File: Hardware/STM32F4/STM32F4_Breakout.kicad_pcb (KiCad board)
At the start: 4 copper layers, 68 x 59 mm, 50 parts, among them J1 Screw_Terminal_01x02, J2 SWD, J3 Conn_01x04, J4 Conn_01x04, J5 USB_B, Q1 AO3401A, SW1 SW_SPDT, U1 STM32F405RGT6, U2 MP2303ADN, U3 USBLC6-2SC6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

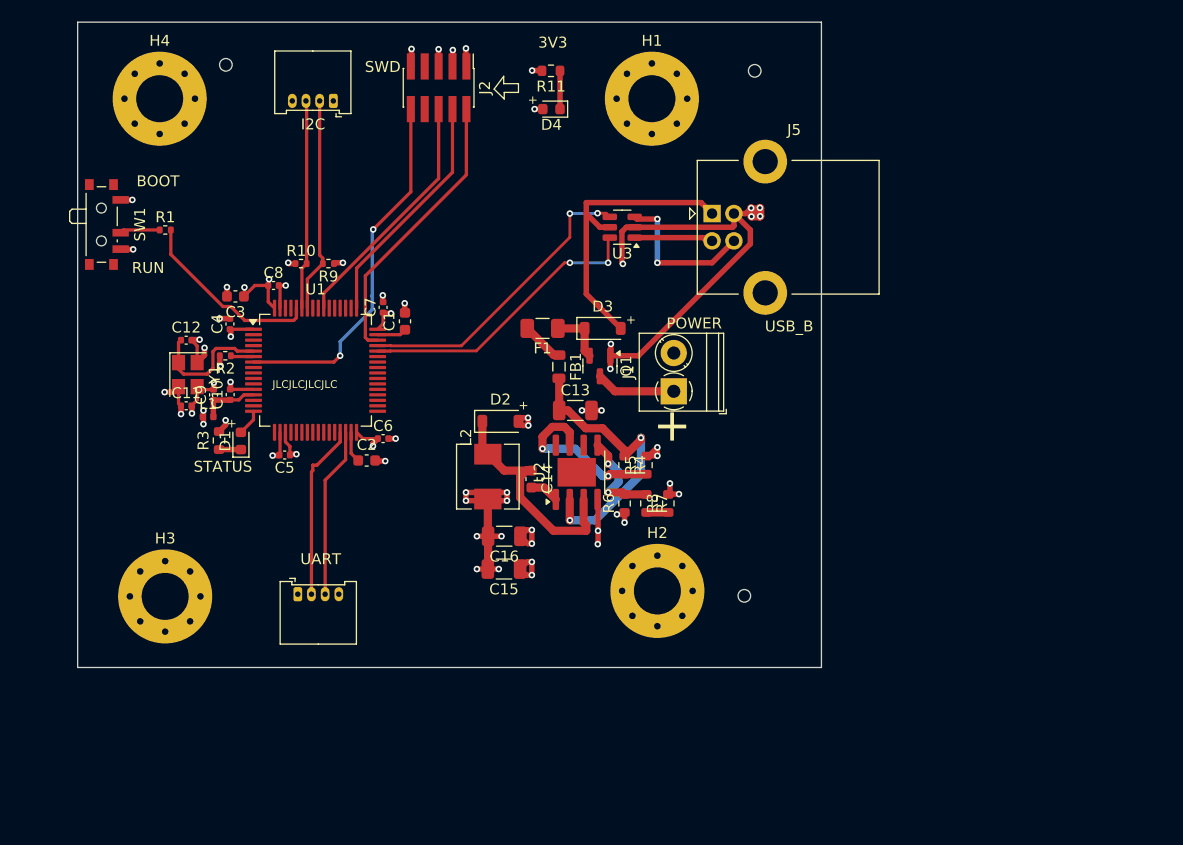
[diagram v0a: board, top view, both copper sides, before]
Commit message: Consolidated Kicad projects
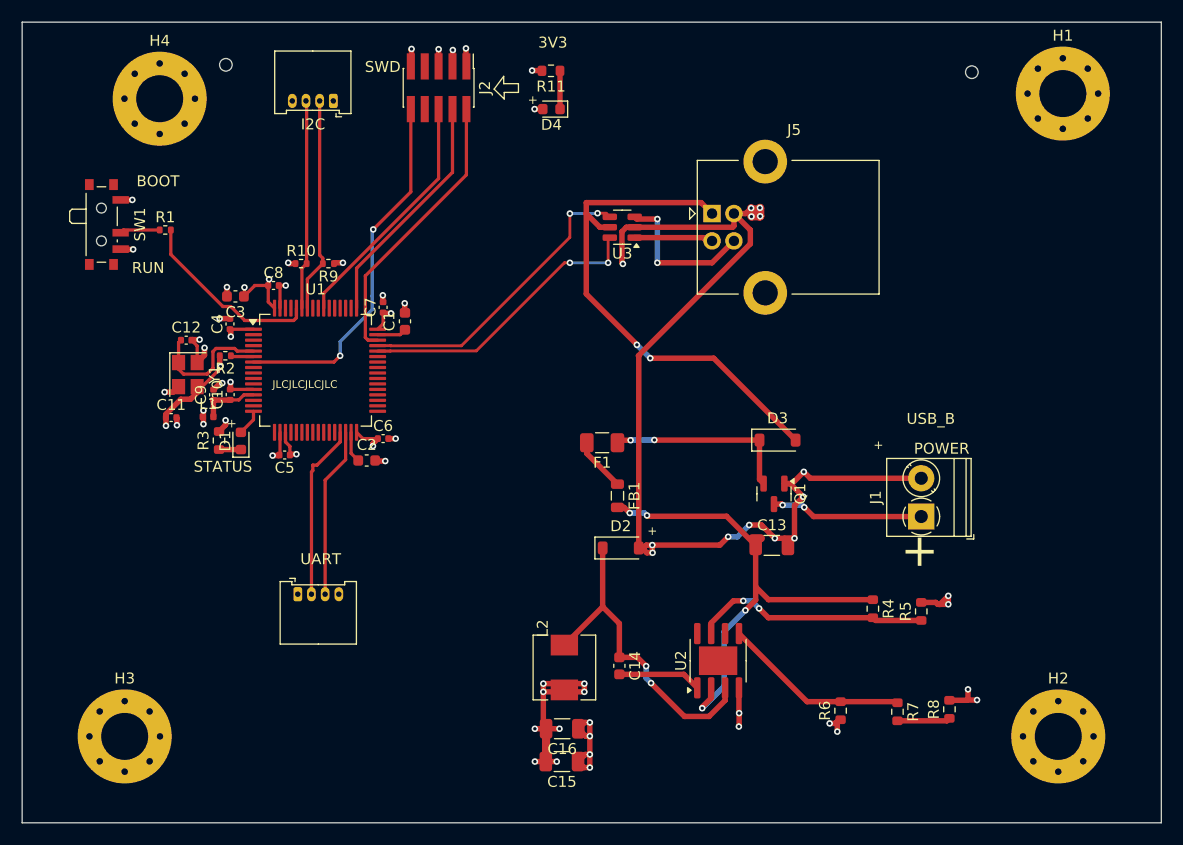
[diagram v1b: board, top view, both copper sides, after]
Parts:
- moved H2 39.0 mm to (140.2, 139.3)
- moved H1 37.6 mm to (140.6, 80.5)
- moved R8 31.9 mm to (130.2, 136.8)
- moved R7 29.8 mm to (125.5, 137.1)
- moved R5 28.5 mm to (127.6, 127.9)
- moved R6 27.4 mm to (120.2, 136.9)
- moved R4 26.2 mm to (123.2, 127.6)
- moved J1 25.4 mm to (127.6, 119.2)
- moved C13 21.8 mm to (114.0, 121.8)
- moved U2 21.5 mm to (109.1, 132.4)
- moved Q1 19.7 mm to (114.2, 117.1)
- moved D3 19.0 mm to (114.5, 112.2)
- moved C14 18.9 mm to (100.0, 132.8)
- moved L2 18.8 mm to (95.0, 133.0)
- moved C15 18.4 mm to (94.8, 141.6)
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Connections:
- C11 pad 1: GND -> Net-(C11-Pad1)
- R2 pad 2: GND -> Net-(C11-Pad1)
- Y1 pad 3: GND -> Net-(C11-Pad1)
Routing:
- net GND: track 101.6 -> 143.6 mm
- net +5V: track 27.4 -> 47.6 mm, vias 0 -> 2
- net BUCK_IN: track 27.3 -> 45.2 mm, vias 2 -> 4
- net Net-(D3-K): track 5.28 -> 17.4 mm, vias 0 -> 2
- net Net-(C11-Pad1): track 0.00 -> 9.66 mm, vias 0 -> 2
- net BUCK_SW: track 21.3 -> 29.9 mm, vias 0 -> 2
- net BUCK_FB: track 9.21 -> 17.1 mm, vias 2 -> 0
- net +12V: track 7.32 -> 13.9 mm, vias 0 -> 2
- net BUCK_EN: track 16.5 -> 21.8 mm
- net BUCK_BS: track 2.67 -> 7.64 mm
- net Net-(R7-Pad2): track 2.00 -> 4.84 mm
- net Net-(F1-Pad2): track 3.91 -> 4.95 mm
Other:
- board size 68 x 59 mm -> 104.1 x 73.2 mm

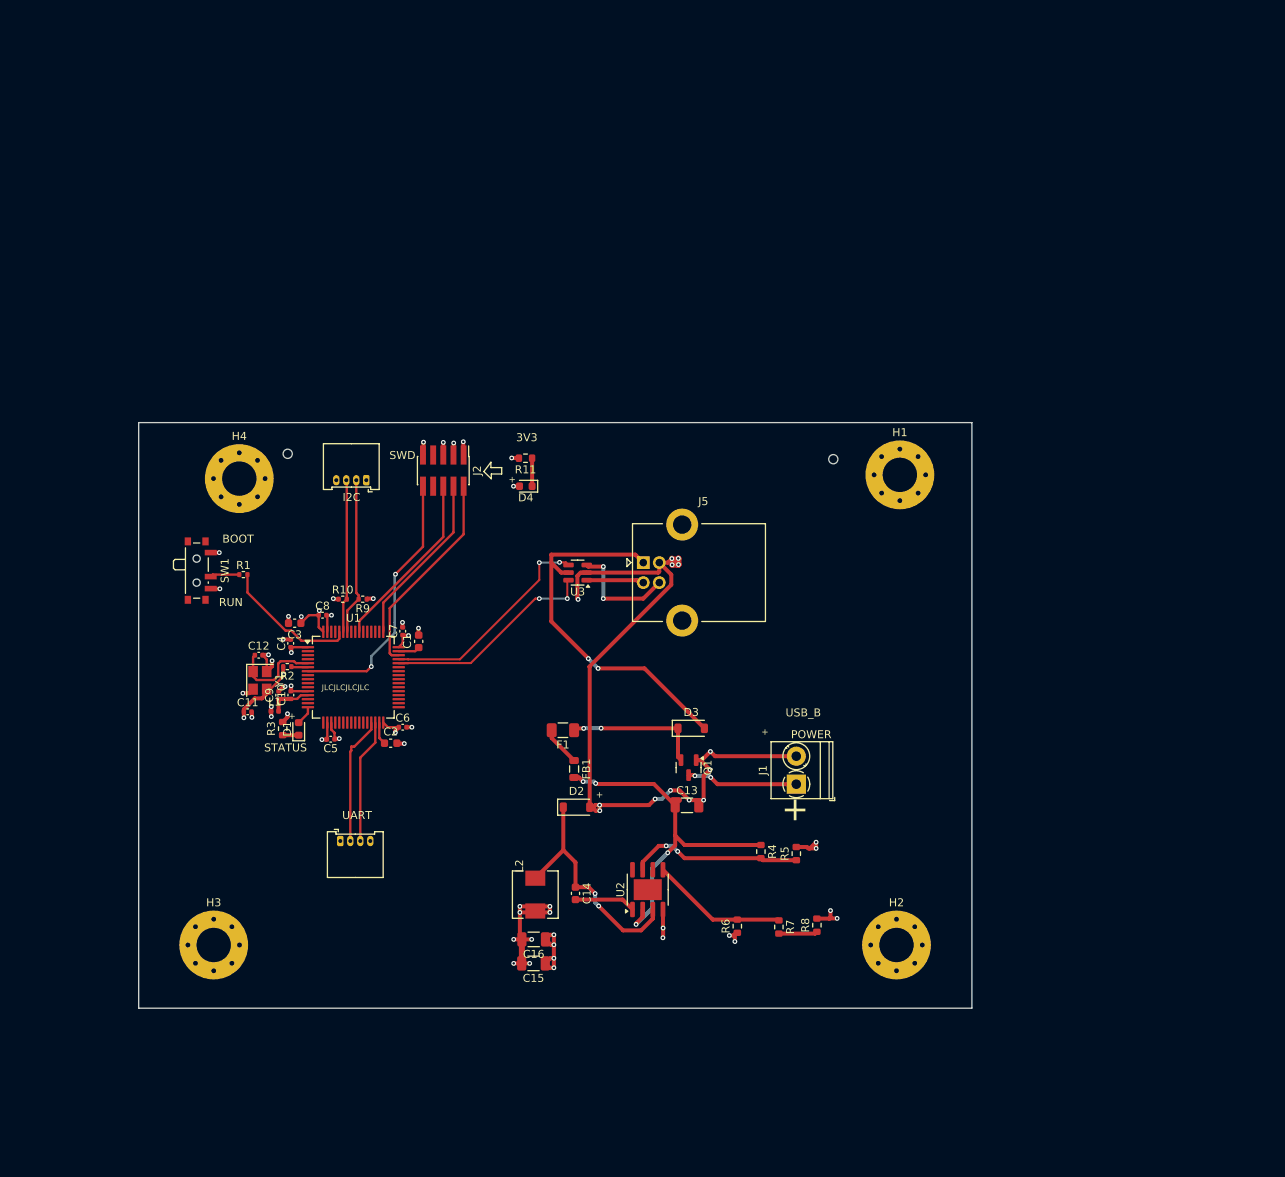
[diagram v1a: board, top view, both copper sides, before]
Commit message: CAN transceiver
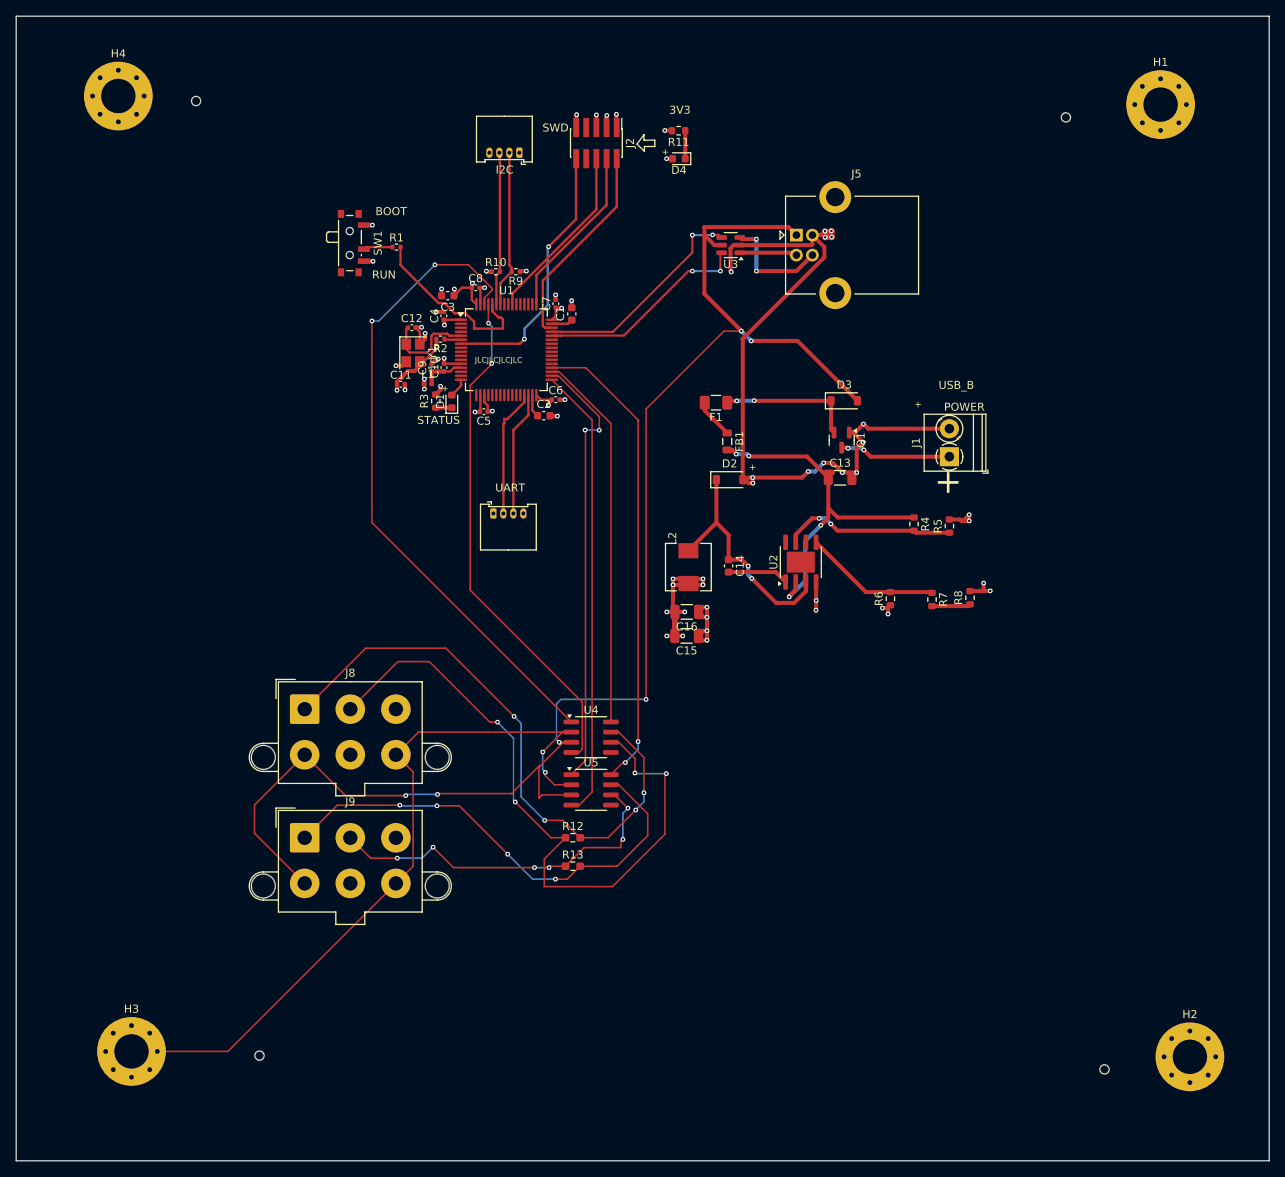
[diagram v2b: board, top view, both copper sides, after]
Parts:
- added J8: CAN Connector1, Connector_Molex:Molex_Mega-Fit_76829-0006_2x03_P5.70mm_Vertical, F.Cu at (66.2, 109.8)
- added J9: CAN Connector2, Connector_Molex:Molex_Mega-Fit_76829-0006_2x03_P5.70mm_Vertical, F.Cu at (66.2, 125.9)
- added R12: 120, Resistor_SMD:R_0603_1608Metric_Pad0.98x0.95mm_HandSolder, F.Cu at (99.7, 125.9)
- added R13: 120, Resistor_SMD:R_0603_1608Metric_Pad0.98x0.95mm_HandSolder, F.Cu at (99.7, 129.4)
- added U4: TJA1051T, Package_SO:SOIC-8_3.9x4.9mm_P1.27mm, F.Cu at (102.0, 113.3)
- added U5: TJA1051T, Package_SO:SOIC-8_3.9x4.9mm_P1.27mm, F.Cu at (102.0, 119.9)
- moved H1 56.6 mm to (173.2, 34.2)
- moved H4 50.2 mm to (42.9, 33.2)
- moved R7 45.2 mm to (144.6, 96.1)
- moved Q1 45.2 mm to (133.3, 76.2)
- moved C10 45.2 mm to (83.6, 67.1)
- moved C11 45.2 mm to (78.2, 69.2)
- moved C12 45.2 mm to (79.6, 62.1)
- moved C16 45.2 mm to (113.9, 97.7)
- moved C2 45.2 mm to (96.1, 73.1)
- moved C3 45.2 mm to (84.1, 58.1)
- moved C4 45.2 mm to (83.6, 60.7)
- moved C5 45.2 mm to (88.6, 72.6)
- moved C6 45.2 mm to (97.6, 71.1)
- moved C7 45.2 mm to (97.6, 59.1)
- moved C8 45.2 mm to (87.5, 57.1)
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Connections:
- U1 pad 35: unconnected-(U1-PB14-Pad35) -> CAN SIlent Mode 1
- U1 pad 36: unconnected-(U1-PB15-Pad36) -> CAN SIlent Mode 2
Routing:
- net +5V: track 47.6 -> 185.6 mm, vias 2 -> 6
- net GND: track 143.6 -> 237.7 mm, vias 43 -> 45
- net CAN1-: track 0.00 -> 85.5 mm, vias 0 -> 4
- net CAN1_TX: track 0.00 -> 82.0 mm, vias 0 -> 2
- net CAN1+: track 0.00 -> 73.6 mm, vias 0 -> 4
- net CAN1_RX: track 0.00 -> 64.2 mm, vias 0 -> 2
- net CAN2+: track 0.00 -> 59.5 mm, vias 0 -> 4
- net CAN SIlent Mode 2: track 0.00 -> 59.5 mm, vias 0 -> 2
- net CAN2_RX: track 0.00 -> 56.9 mm
- net CAN2_TX: track 0.00 -> 55.4 mm, vias 0 -> 2
- net CAN SIlent Mode 1: track 0.00 -> 47.4 mm
- net CAN2-: track 0.00 -> 45.6 mm, vias 0 -> 6
- net BOOT0: track 17.2 -> 22.6 mm
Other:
- board size 104.1 x 73.2 mm -> 156.6 x 143.1 mm
